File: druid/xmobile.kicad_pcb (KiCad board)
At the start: 2 copper layers, 99 parts, among them CON1 AVR-PDI-6, IC1 ATXMEGA128A4U-A, P1 USB_B, P2 CONN_01X02, P3 CONN_8, P4 CONN_MICROPHONE, P5 CONN_MICROPHONE, P6 CONN_10, P7 CONN_4, P8 CONN_01X02, P9 CONN_01X02, Q1 A2SHB, Q2 A2SHB, U1 STF202-22T1G, U10 switch1, U11 switch1, U12 switch1, U13 switch1, U14 switch1, U2 SIM800C, U3 MOLEX_SIM_HOLDER_47553, U4 XC6206P332MR, U5 switch1, U6 switch1, U7 switch1, U8 switch1, U9 switch1

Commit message: Теперь все площадки разложены по кучкам
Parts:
- moved D10 45.0 mm to (225.6, 47.8), turned to 180 degrees
- moved C23 41.5 mm to (238.8, 44.7), turned to 180 degrees
- moved C22 33.4 mm to (231.1, 47.8), turned to 90 degrees
- moved R7 27.9 mm to (127.0, 125.0)
- moved U4 27.1 mm to (58.4, 128.9), turned to 90 degrees
- moved L2 26.8 mm to (57.8, 120.7), turned to 270 degrees
- moved R16 26.2 mm to (127.0, 129.5)
- moved R15 26.1 mm to (92.5, 130.6), turned to 270 degrees
- moved L1 26.0 mm to (57.8, 111.1), turned to 270 degrees
- moved R9 25.6 mm to (115.8, 138.2), turned to 270 degrees
- moved R12 25.2 mm to (92.5, 136.7), turned to 270 degrees
- moved C2 24.2 mm to (59.7, 102.2), turned to 180 degrees
- moved R14 23.9 mm to (89.4, 130.6), turned to 270 degrees
- moved P8 23.4 mm to (162.6, 29.2)
- moved R11 23.0 mm to (89.4, 136.7), turned to 90 degrees
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
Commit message: Заменил посадочные места для некоторых контактных расчёсок
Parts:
- P4: footprint Connectors_Molex:Molex_KK-6410-02_02x2.54mm_Straight -> Connectors_Hirose:Hirose_DF13-02P-1.25DSA_02x1.25mm_Straight
- P7: footprint Connectors_Molex:Molex_KK-6410-04_04x2.54mm_Straight -> Connectors_JAE:JAE_LY20-04P-2T_2x02x2.00mm_Straight
- P8, P9: footprint Connectors_Molex:Molex_KK-6410-02_02x2.54mm_Straight -> Connectors_JAE:JAE_LY20-08P-2T_2x04x2.00mm_Straight

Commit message: Соединеты проводникаи отдельные блоки и начато подключение SIM800 к XMEGA
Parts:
- added C32: 100nF, Capacitors_SMD:C_0603_HandSoldering, F.Cu at (118.0, 42.2)
- added C33: 100nF, Capacitors_SMD:C_0603_HandSoldering, F.Cu at (118.0, 37.2)
- added C34: 100nF, Capacitors_SMD:C_0603_HandSoldering, F.Cu at (90.6, 43.2)
- added C35: 100nF, Capacitors_SMD:C_0603_HandSoldering, F.Cu at (118.0, 47.2)
- added C36: 100nF, Capacitors_SMD:C_0603_HandSoldering, F.Cu at (108.2, 59.5)
- added C37: 100nF, Capacitors_SMD:C_0603_HandSoldering, F.Cu at (91.0, 48.2)
- added C38: 100nF, Capacitors_SMD:C_0603_HandSoldering, F.Cu at (102.1, 29.9)
- added C39: 100nF, Capacitors_SMD:C_0603_HandSoldering, F.Cu at (90.7, 38.2)
- added C40: 10mk, Capacitors_SMD:c_elec_4x5.3, F.Cu at (102.3, 26.0)
- added C41: 10mk, Capacitors_SMD:c_elec_4x5.3, F.Cu at (89.8, 34.4)
- added P10: CONN_01X08, Connectors_JAE:JAE_LY20-08P-2T_2x04x2.00mm_Straight, F.Cu at (158.5, 59.5)
- C2: value 10mk -> 100nF; footprint Capacitors_SMD:c_elec_4x5.3 -> Capacitors_SMD:C_0603_HandSoldering
- C3: value 100n -> 100nF; footprint Capacitors_SMD:C_1206_HandSoldering -> Capacitors_SMD:C_0603_HandSoldering
- C31: footprint Capacitors_SMD:C_1206_HandSoldering -> Capacitors_SMD:C_0603_HandSoldering
- IC1: value ATXMEGA128A4U-A -> ATXMEGA128A1U-A; footprint tqfp:TQFP-44_10x10mm_Pitch0.8mm -> tqfp:LQFP-100_14x14mm_Pitch0.5mm
- P2: footprint Connectors_Hirose:Hirose_DF13-02P-1.25DS_02x1.25mm_Angled -> Connectors_JAE:JAE_LY20-04P-2T_2x02x2.00mm_Straight
- P4: footprint Connectors_Hirose:Hirose_DF13-02P-1.25DSA_02x1.25mm_Straight -> Connectors_JAE:JAE_LY20-04P-2T_2x02x2.00mm_Straight
- P5: footprint Connectors_Molex:Molex_KK-6410-02_02x2.54mm_Straight -> Connectors_JAE:JAE_LY20-04P-2T_2x02x2.00mm_Straight
- P6: footprint Connectors_Hirose:Hirose_DF13-10P-1.25DSA_10x1.25mm_Straight -> Connectors_JAE:JAE_LY20-10P-2T_2x05x2.00mm_Straight
- P8, P9: footprint Connectors_JAE:JAE_LY20-08P-2T_2x04x2.00mm_Straight -> Connectors_JAE:JAE_LY20-04P-2T_2x02x2.00mm_Straight
- moved C1 221.5 mm to (265.3, 143.4)
- moved U1 217.2 mm to (270.7, 143.0)
- moved P1 217.0 mm to (270.4, 151.3)
- moved R21 173.7 mm to (83.7, 162.6)
- moved U6 170.3 mm to (93.5, 164.6)
- moved D11 164.2 mm to (47.3, 145.1), turned to 0 degrees
- moved D1 160.4 mm to (118.8, 67.3)
- moved C27 151.8 mm to (47.1, 133.9)
- moved P8 151.8 mm to (45.8, 126.3)
- moved R5 151.4 mm to (123.0, 67.3)
- moved C28 150.2 mm to (47.1, 136.5)
- moved U10 149.4 mm to (108.0, 175.0)
- moved U13 149.4 mm to (123.3, 175.1)
- moved C26 148.7 mm to (47.1, 139.1)
- moved R22 147.6 mm to (83.5, 172.9)
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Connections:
- C2 pad 1: Net-(C2-Pad1) -> GND
- C2 pad 2: GND -> /3.3V
- C3 pad 2: Net-(C2-Pad1) -> /3.3V
- CON1 pad 3: Net-(CON1-Pad3) -> (no net)
- CON1 pad 4: Net-(CON1-Pad4) -> (no net)
- D10 pad 3: Net-(D10-Pad3) -> (no net)
- IC1 pad 1: /XMEGA_PA5 -> /XMEGA_PA6
- IC1 pad 10: /KBD_OUT_1 -> (no net)
- IC1 pad 11: /KBD_OUT_2 -> (no net)
- IC1 pad 12: /KBD_OUT_3 -> (no net)
- IC1 pad 13: /XMEGA_PC3 -> GND
- IC1 pad 14: /EPD_CS -> /3.3V
- IC1 pad 15: /EPD_DIN -> /KBD_OUT_1
- IC1 pad 16: /XMEGA_PC6 -> /KBD_OUT_2
- IC1 pad 17: /EPD_CLK -> /KBD_OUT_3
- IC1 pad 18: GND -> /XMEGA_PC3
- IC1 pad 19: /3.3V -> /EPD_CS
- IC1 pad 2: /XMEGA_PA6 -> /XMEGA_PA7
- IC1 pad 20: /XMEGA_PD0_GSM_POWER -> /EPD_DIN
- IC1 pad 21: /XMEGA_PD1_GPIO -> /XMEGA_PC6
- IC1 pad 22: /XMEGA_PD2_GPIO -> /EPD_CLK
- IC1 pad 23: /XMEGA_PD3_GPIO -> GND
- IC1 pad 24: /XMEGA_PD4_GPIO -> /3.3V
- IC1 pad 25: /KBD_IN_1 -> /XMEGA_PD0_GSM_POWER
- IC1 pad 26: /KBD_IN_2 -> /XMEGA_PD1_GPIO
- IC1 pad 27: /KBD_IN_3 -> /XMEGA_PD2_GPIO
- IC1 pad 28: /XMEGA_PE0_GPIO -> /XMEGA_PD3_GPIO
- IC1 pad 29: Net-(IC1-Pad29) -> /XMEGA_PD4_GPIO
- IC1 pad 3: /XMEGA_PA7 -> GND
- IC1 pad 30: GND -> /KBD_IN_1
- IC1 pad 31: /3.3V -> /KBD_IN_2
- IC1 pad 32: /XMEGA_PE2_RXD0 -> /KBD_IN_3
- IC1 pad 33: /XMEGA_PE3_TXD0 -> GND
- IC1 pad 34: /PDI_D -> /3.3V
- IC1 pad 35: /PDI_C -> /XMEGA_PE0_GPIO
- IC1 pad 36: /XMEGA_PR0 -> (no net)
- IC1 pad 37: /XMEGA_PR1 -> /XMEGA_PE2_RXD0
- IC1 pad 38: GND -> /XMEGA_PE3_TXD0
- IC1 pad 39: Net-(C2-Pad1) -> (no net)
- IC1 pad 4: /XMEGA_PB0 -> Net-(C38-Pad2)
- IC1 pad 40: /XMEGA_PA0 -> (no net)
- IC1 pad 41: /EPD_DC -> (no net)
- IC1 pad 42: /XMEGA_PA2 -> (no net)
- IC1 pad 43: /EPD_BUSY -> GND
- IC1 pad 44: /EPD_RST -> /3.3V
- IC1 pad 5: /XMEGA_PB1 -> /XMEGA_PB0
- IC1 pad 6: /XMEGA_PB2 -> /XMEGA_PB1
- IC1 pad 7: /XMEGA_PB3 -> /XMEGA_PB2
- IC1 pad 8: GND -> /XMEGA_PB3
- IC1 pad 9: /3.3V -> (no net)
- L1 pad 1: Net-(C2-Pad1) -> Net-(C38-Pad2)
- P2 pad 2: Net-(P2-Pad2) -> (no net)
- P7 pad 4: Net-(P7-Pad4) -> (no net)
- U10 pad 3: Net-(U10-Pad3) -> (no net)
- U11 pad 3: Net-(U11-Pad3) -> (no net)
- U12 pad 2: Net-(U12-Pad2) -> (no net)
- U12 pad 3: Net-(U12-Pad3) -> (no net)
- U13 pad 2: Net-(U13-Pad2) -> (no net)
- U13 pad 3: Net-(U13-Pad3) -> (no net)
- U14 pad 2: Net-(U14-Pad2) -> (no net)
- U14 pad 3: Net-(U14-Pad3) -> (no net)
- U2 pad 20: Net-(U2-Pad20) -> (no net)
- U2 pad 22: Net-(U2-Pad22) -> (no net)
- U2 pad 23: Net-(U2-Pad23) -> (no net)
- U2 pad 28: Net-(U2-Pad28) -> (no net)
- U2 pad 29: Net-(U2-Pad29) -> (no net)
- U2 pad 38: Net-(U2-Pad38) -> (no net)
- U2 pad 42: Net-(U2-Pad42) -> (no net)
- U3 pad 4: Net-(U3-Pad4) -> (no net)
- U5 pad 2: Net-(U5-Pad2) -> (no net)
- U5 pad 3: Net-(U5-Pad3) -> (no net)
- U6 pad 3: Net-(U6-Pad3) -> (no net)
- U7 pad 3: Net-(U7-Pad3) -> (no net)
- U8 pad 3: Net-(U8-Pad3) -> (no net)
- U9 pad 3: Net-(U9-Pad3) -> (no net)
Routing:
- net GND: track 0.00 -> 64.6 mm
- net /3.3V: track 0.00 -> 61.0 mm
- net /GSM_AT_RI: track 0.00 -> 54.1 mm
- net /GSM_AT_DTR: track 0.00 -> 51.4 mm, vias 0 -> 2
- net /GSM_AT_DCD: track 0.00 -> 49.5 mm
- net /GSM_AT_CTS: track 0.00 -> 47.4 mm
- net Net-(D10-Pad6): track 0.00 -> 45.7 mm, vias 0 -> 2
- net /GSM_AT_RTS: track 0.00 -> 44.2 mm
- net Net-(D10-Pad5): track 0.00 -> 39.8 mm
- net Net-(R25-Pad2): track 0.00 -> 38.3 mm, vias 0 -> 4
- net Net-(R26-Pad2): track 0.00 -> 38.2 mm
- net Net-(R24-Pad2): track 0.00 -> 37.0 mm, vias 0 -> 4
- net /GSM_SPKP: track 0.00 -> 32.2 mm
- net /GSM_AT_TXD: track 0.00 -> 31.7 mm
- net /GSM_SPKN: track 0.00 -> 31.1 mm
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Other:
- net class Default: trace_width 0.25 -> 0.75

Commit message: Всё разведено кроме земель. Площидки надо проверять.
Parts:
- removed P6: CONN_10, Connectors_JAE:JAE_LY20-10P-2T_2x05x2.00mm_Straight
- moved D2 167.0 mm to (76.6, 95.2)
- moved D3 167.0 mm to (76.6, 98.4)
- moved D6 167.0 mm to (74.7, 95.2)
- moved D7 167.0 mm to (74.7, 98.4)
- moved P4 167.0 mm to (67.6, 95.9)
- moved C16 167.0 mm to (78.5, 91.2)
- moved C17 167.0 mm to (80.5, 97.0)
- moved C18 167.0 mm to (78.5, 102.5)
- moved C10 159.7 mm to (98.6, 97.6)
- moved C11 159.7 mm to (103.9, 99.6)
- moved C12 159.7 mm to (98.7, 101.6)
- moved C4 141.4 mm to (93.7, 112.5), turned to 0 degrees
- moved C7 137.8 mm to (93.7, 109.4), turned to 0 degrees
- moved P8 136.1 mm to (168.6, 67.7), turned to 270 degrees
- moved C5 135.6 mm to (101.3, 112.4), turned to 0 degrees
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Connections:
- IC1 pad 1: /XMEGA_PA6 -> (no net)
- IC1 pad 100: /XMEGA_PA5 -> (no net)
- IC1 pad 18: /XMEGA_PC3 -> (no net)
- IC1 pad 2: /XMEGA_PA7 -> (no net)
- IC1 pad 5: /XMEGA_PB0 -> (no net)
- IC1 pad 6: /XMEGA_PB1 -> (no net)
- IC1 pad 7: /XMEGA_PB2 -> (no net)
- IC1 pad 8: /XMEGA_PB3 -> (no net)
- IC1 pad 91: /XMEGA_PR0 -> (no net)
- IC1 pad 92: /XMEGA_PR1 -> (no net)
- R21 pad 2: /KBD_OUT_1 -> /KBD_OUT_3
- R23 pad 2: /KBD_OUT_3 -> /KBD_OUT_1
- R24 pad 1: /KBD_IN_1 -> /KBD_IN_3
- R26 pad 1: /KBD_IN_3 -> /KBD_IN_1
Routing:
- net /3.3V: track 61.0 -> 193.9 mm
- net /KBD_OUT_1: track 0.00 -> 107.8 mm
- net /KBD_OUT_2: track 0.00 -> 94.0 mm
- net /KBD_IN_3: track 0.00 -> 89.1 mm, vias 0 -> 2
- net +BATT: track 16.7 -> 99.2 mm
- net /XMEGA_PD0_GSM_POWER: track 0.00 -> 82.3 mm, vias 0 -> 2
- net /KBD_OUT_3: track 0.00 -> 80.5 mm
- net /GSM_SPKN: track 31.1 -> 107.3 mm
- net /GSM_SPKP: track 32.2 -> 107.6 mm
- net /KBD_IN_2: track 0.00 -> 70.8 mm, vias 0 -> 2
- net /SIM_HOLDER_VDD_EXT: track 0.00 -> 62.9 mm, vias 0 -> 2
- net /EPD_CLK: track 0.00 -> 62.1 mm, vias 0 -> 2
- net /EPD_DIN: track 0.00 -> 61.6 mm, vias 0 -> 2
- net /GSM_USB_VBUS: track 14.3 -> 67.8 mm
- net /KBD_IN_1: track 0.00 -> 53.1 mm, vias 0 -> 2
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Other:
- net class Default: trace_width 0.75 -> 0.25

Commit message: Ground lines and poligones are completed.
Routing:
- net GND: track 85.9 -> 614.0 mm, vias 0 -> 53
- net /GSM_ANT: track 0.00 -> 6.36 mm
- added copper zone on B.Cu, net GND

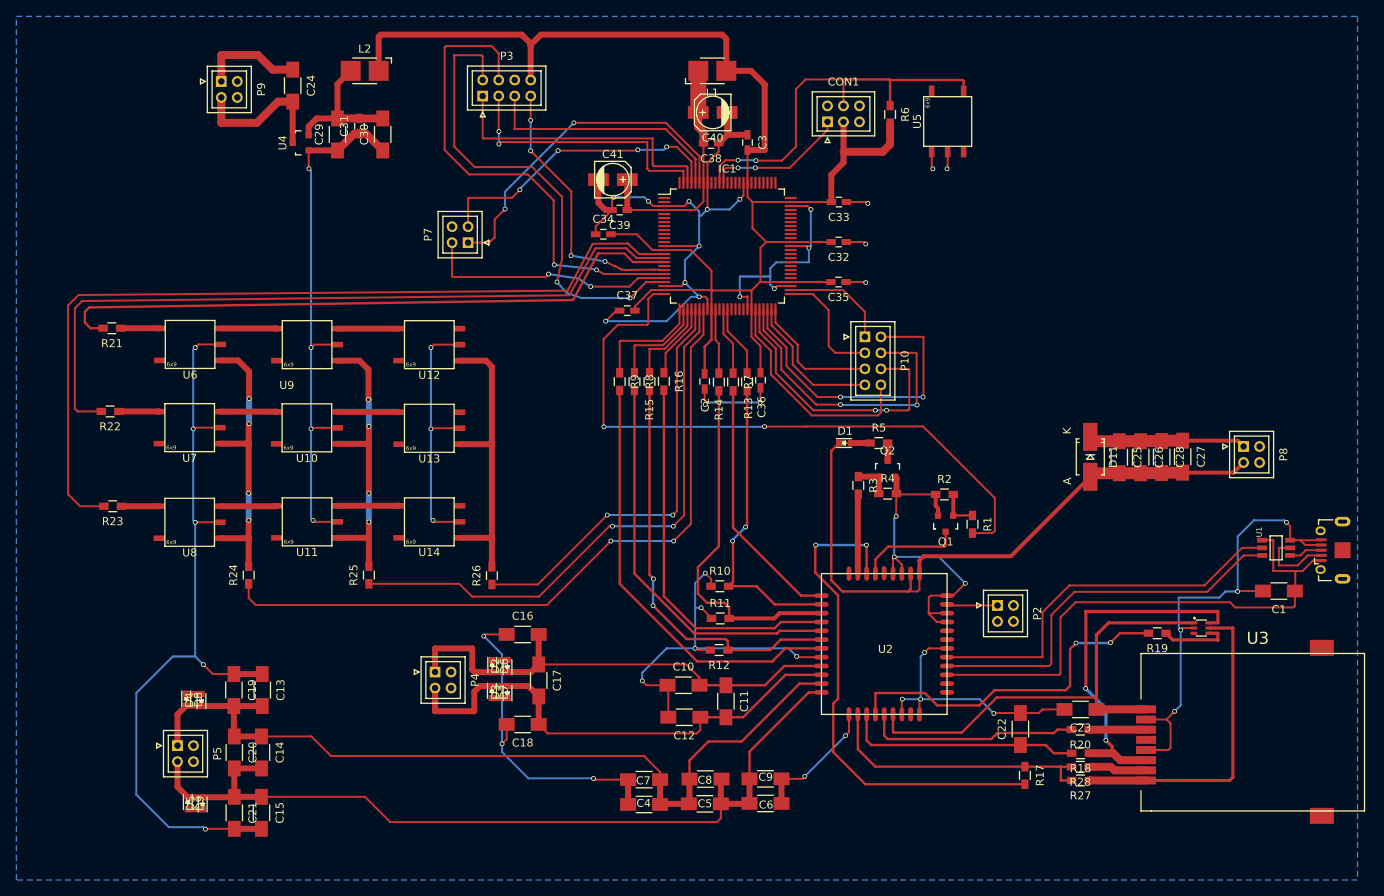
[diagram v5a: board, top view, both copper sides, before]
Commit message: Added board borders on Edge.cuts layer. Added size of board. Created Gerber files (and sent to https://jlcpcb.com for manufacturing)
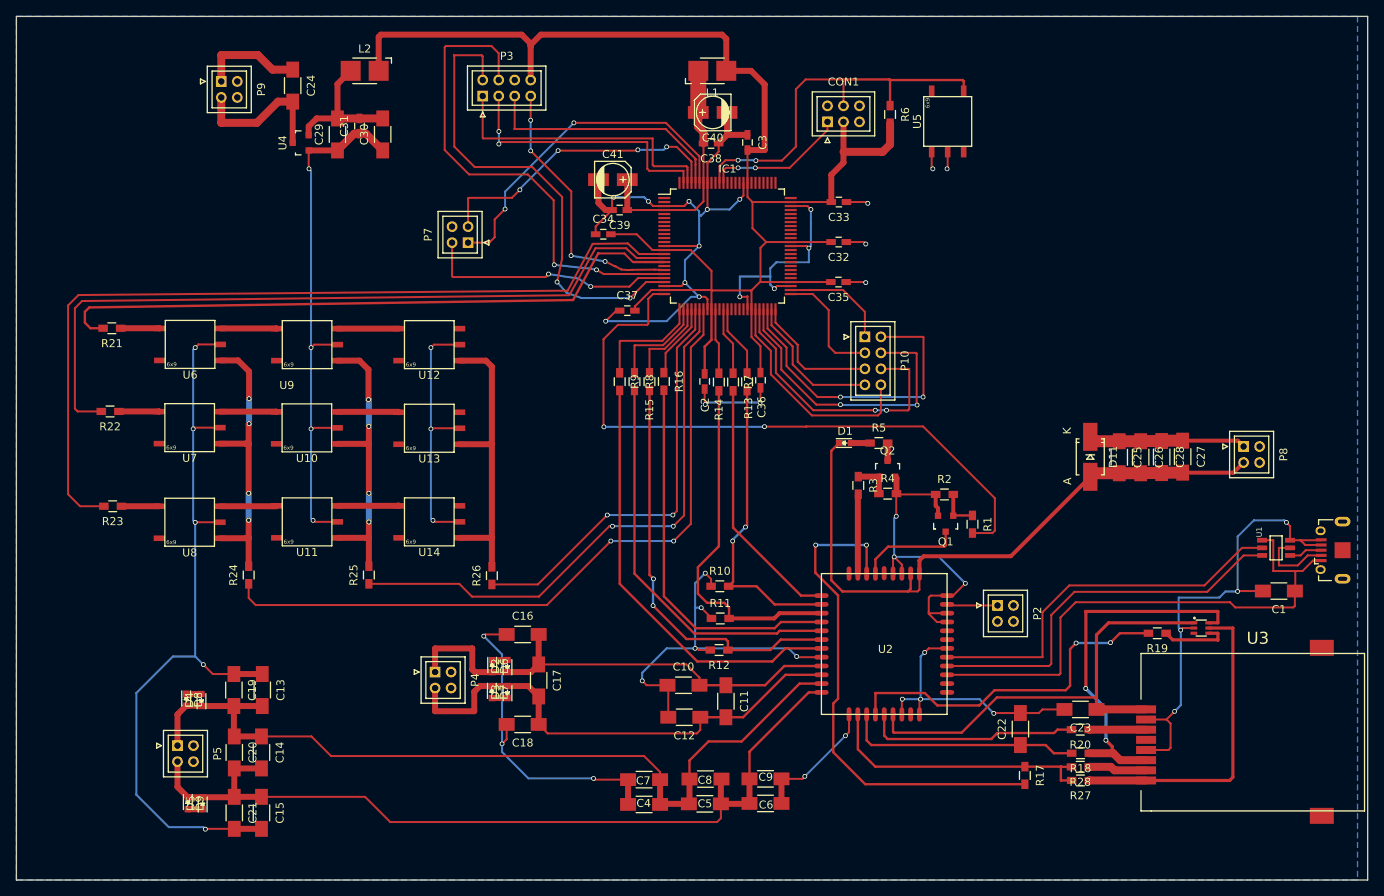
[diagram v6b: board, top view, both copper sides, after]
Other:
- board outline added: 168.9 x 108 mm
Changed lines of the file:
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@@
-(kicad_pcb (version 4) (host pcbnew 4.0.7)
+(kicad_pcb (version 4) (host pcbnew 4.0.2+dfsg1-stable)
   (general
     (links 262)
     (no_connects 1)
-    (area 15.24 13.97 185.199286 121.920001)
+    (area 15.189999 3.5 203.024286 121.970001)
     (thickness 1.6)
-    (drawings 0)
+    (drawings 7)
     (tracks 1109)
     (zones 0)
@@
   (layers
     (0 F.Cu signal)
-    (31 B.Cu signal)
+    (31 B.Cu signal hide)
     (32 B.Adhes user)
     (33 F.Adhes user)
@@
     (visible_elements FFFEFF7F)
     (pcbplotparams
-      (layerselection 0x00030_80000001)
+      (layerselection 0x010f0_80000001)
       (usegerberextensions false)
-      (excludeedgelayer true)
-      (linewidth 0.100000)
+      (usegerberattributes true)
+      (excludeedgelayer false)
+      (linewidth 0.150000)
       (plotframeref false)
       (viasonmask false)
       (mode 1)
-      (useauxorigin false)
+      (useauxorigin true)
       (hpglpennumber 1)
       (hpglpenspeed 20)
@@
       (outputformat 1)
       (mirror false)
-      (drillshape 1)
+      (drillshape 0)
       (scaleselection 1)
-      (outputdirectory ""))
+      (outputdirectory gerbers/))
   )
   (net 0 "")
@@
     )
   )
+  (dimension 107.95 (width 0.3) (layer Dwgs.User)
+    (gr_text "107,950 mm" (at 195.66 67.945 90) (layer Dwgs.User)
+      (effects (font (size 1.5 1.5) (thickness 0.3)))
+    )
+    (feature1 (pts (xy 184.15 13.97) (xy 197.01 13.97)))
+    (feature2 (pts (xy 184.15 121.92) (xy 197.01 121.92)))
+    (crossbar (pts (xy 194.31 121.92) (xy 194.31 13.97)))
+    (arrow1a (pts (xy 194.31 13.97) (xy 194.896421 15.096504)))
+    (arrow1b (pts (xy 194.31 13.97) (xy 193.723579 15.096504)))
+    (arrow2a (pts (xy 194.31 121.92) (xy 194.896421 120.793496)))
+    (arrow2b (pts (xy 194.31 121.92) (xy 193.723579 120.793496)))
+  )
+  (dimension 168.91 (width 0.3) (layer Dwgs.User)
+    (gr_text "168,910 mm" (at 99.695 5) (layer Dwgs.User)
+      (effects (font (size 1.5 1.5) (thickness 0.3)))
+    )
+    (feature1 (pts (xy 184.15 13.97) (xy 184.15 3.65)))
+    (feature2 (pts (xy 15.24 13.97) (xy 15.24 3.65)))
+    (crossbar (pts (xy 15.24 6.35) (xy 184.15 6.35)))
+    (arrow1a (pts (xy 184.15 6.35) (xy 183.023496 6.936421)))
+    (arrow1b (pts (xy 184.15 6.35) (xy 183.023496 5.763579)))
+    (arrow2a (pts (xy 15.24 6.35) (xy 16.366504 6.936421)))
+    (arrow2b (pts (xy 15.24 6.35) (xy 16.366504 5.763579)))
+  )
+  (gr_line (start 184.15 121.92) (end 15.24 121.92) (angle 90) (layer Edge.Cuts) (width 0.1))
+  (gr_line (start 184.15 13.97) (end 184.15 121.92) (angle 90) (layer Edge.Cuts) (width 0.1))
+  (gr_line (start 182.88 13.97) (end 184.15 13.97) (angle 90) (layer Edge.Cuts) (width 0.1))
+  (gr_line (start 15.24 13.97) (end 182.88 13.97) (angle 90) (layer Edge.Cuts) (width 0.1))
+  (gr_line (start 15.24 121.92) (end 15.24 13.97) (angle 90) (layer Edge.Cuts) (width 0.1))
   (segment (start 175.05 85.8) (end 175.05 87.65) (width 0.25) (layer F.Cu) (net 1))
   (segment (start 145.58 96.27) (end 131.57 96.27) (width 0.25) (layer F.Cu) (net 1))
